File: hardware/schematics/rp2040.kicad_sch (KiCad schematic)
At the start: 36 parts, among them SW1 TS-1088-AR02016, SW2 TS-1088-AR02016, U1 RP2040, U11 AMS1117-3.3_C347222, U2 W25Q128JVSIQTR, X1 X322512MSB4SI

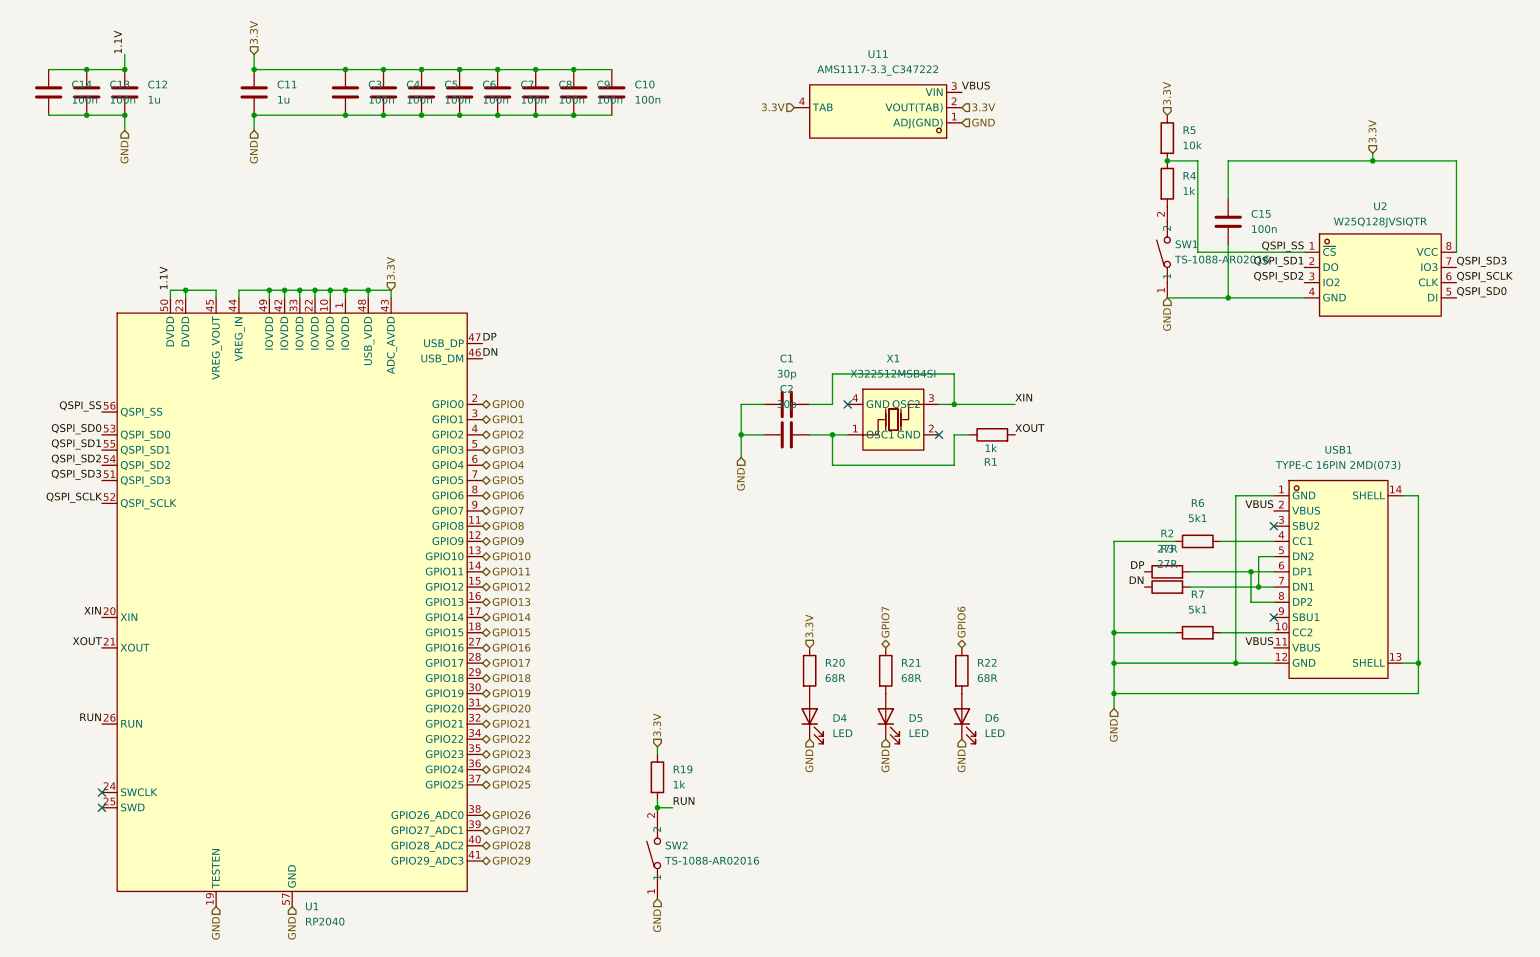
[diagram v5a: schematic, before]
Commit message: Improve trace widths and decoupling
This should improve system stability
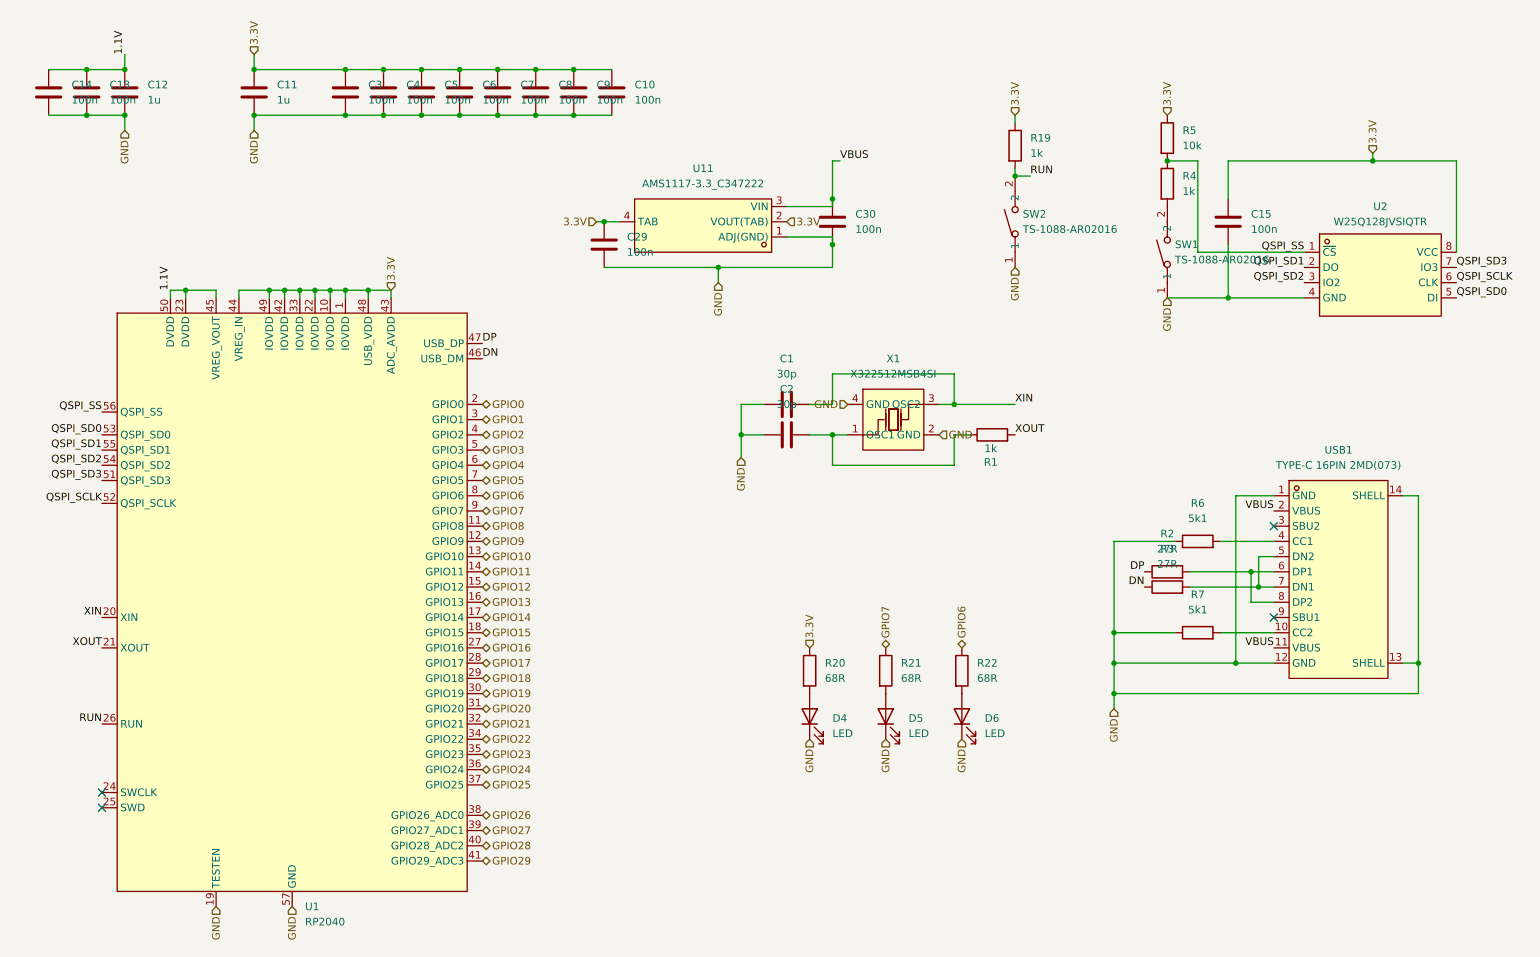
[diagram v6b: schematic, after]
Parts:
- added C29, C30: 100n, Capacitor_SMD:C_0603_1608Metric, symbol Device:C
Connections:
- net 3.3V: now also C29.1
- net GND: now also X1.2 (GND), X1.4 (GND), C29.2, C30.2
- net VBUS: now also C30.1
- no-connect marks 6 -> 4
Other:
- moved on the sheet: R19, SW2, U11
